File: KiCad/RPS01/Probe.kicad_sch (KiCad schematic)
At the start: 10 parts

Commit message: Finished Updating Footprints and Reorganized Reference Designators
Finished Updating Footprints and Reorganized Reference Designators

Starting to work on Final PCB, except for 19V Boost. Please check Schematic for errors
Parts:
- TP1: renamed from TP2; footprint (none) -> Mechatronics TestP:CONN1_RCU-0C_TEC
- TP10: value VSHUNT - -> VSHUNT-; footprint (none) -> Mechatronics TestP:CONN1_RCU-0C_TEC
- TP2: renamed from TP3; footprint (none) -> Mechatronics TestP:CONN1_RCU-0C_TEC
- TP3: renamed from TP4; footprint (none) -> Mechatronics TestP:CONN1_RCU-0C_TEC
- TP4: renamed from TP5; footprint (none) -> Mechatronics TestP:CONN1_RCU-0C_TEC
- TP5: renamed from TP6; footprint (none) -> Mechatronics TestP:CONN1_RCU-0C_TEC
- TP6: renamed from TP7; footprint (none) -> Mechatronics TestP:CONN1_RCU-0C_TEC
- TP7: renamed from TP1; footprint (none) -> Mechatronics TestP:CONN1_RCU-0C_TEC
- TP8: footprint (none) -> Mechatronics TestP:CONN1_RCU-0C_TEC
- TP9: value VSHUNT + -> VSHUNT+; footprint (none) -> Mechatronics TestP:CONN1_RCU-0C_TEC
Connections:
- net VSHUNT + renamed VSHUNT+
- net VSHUNT - renamed VSHUNT-
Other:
- moved on the sheet: TP10, TP9

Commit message: Hotfix
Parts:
- removed TP10: VSHUNT-, Mechatronics TestP:CONN1_RCU-0C_TEC, symbol Connector:TestPoint_Probe
- removed TP9: VSHUNT+, Mechatronics TestP:CONN1_RCU-0C_TEC, symbol Connector:TestPoint_Probe
- renumbered TP8 to TP10, TP1 to TP3, TP2 to TP4, TP3 to TP5, TP4 to TP6, TP5 to TP7, TP6 to TP8, TP7 to TP9

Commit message: Progress
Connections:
- net AREF: no longer TP9.1
- net CURRENT1: no longer TP5.1
- net CURRENT2: no longer TP6.1
- net LOGIC 5V: no longer TP10.1
- net SCL: no longer TP4.1
- net SDA: no longer TP3.1
- net VOLT1: no longer TP7.1
- net VOLT2: no longer TP8.1
- no-connect marks 0 -> 16
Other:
- moved on the sheet: TP10, TP3, TP4, TP5, TP6, TP7, TP8, TP9

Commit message: Error Checker Complete
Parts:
- added TP13: VOLT1, Mechatronics TestP:CONN1_RCU-0C_TEC, symbol Connector:TestPoint_Probe
- added TP14: VOLT2, Mechatronics TestP:CONN1_RCU-0C_TEC, symbol Connector:TestPoint_Probe
- added TP15: AREF, Mechatronics TestP:CONN1_RCU-0C_TEC, symbol Connector:TestPoint_Probe
- added TP16, TP17: LOGIC 5V, Mechatronics TestP:CONN1_RCU-0C_TEC, symbol Connector:TestPoint_Probe
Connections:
- net AREF: now also TP9.1
- net CURRENT1: now also TP5.1
- net CURRENT2: now also TP6.1
- net LOGIC 5V: now also TP10.1
- net SCL: now also TP4.1
- net SDA: now also TP3.1
- net VOLT1: now also TP7.1
- net VOLT2: now also TP8.1
- new net +12V: TP15.1
- new net +19V: TP16.1
- new net +3.3V: TP13.1
- new net +5V: TP14.1
- new net GND: TP17.1
- no-connect marks 16 -> 0

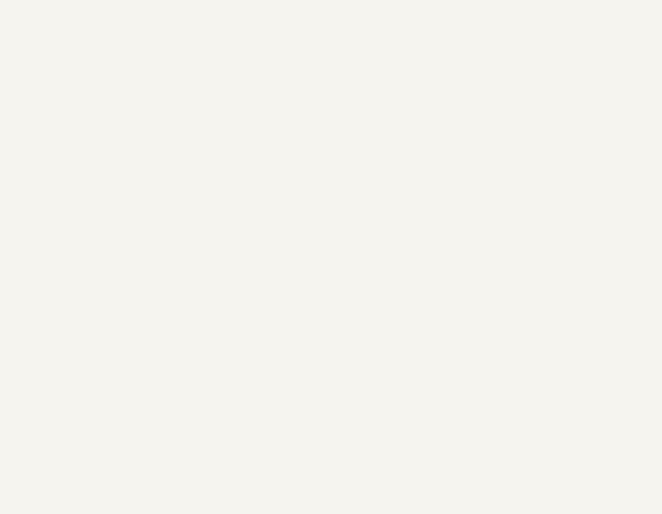
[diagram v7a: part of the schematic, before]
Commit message: Added Proper Mounting Holes and Updated PCB Dimensions
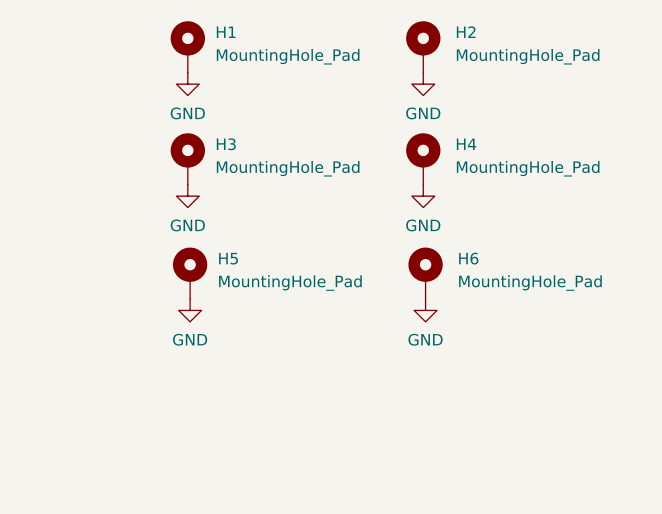
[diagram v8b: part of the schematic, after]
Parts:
- added H1, H2, H3, H4, H5, H6: MountingHole_Pad, MountingHole:MountingHole_3.2mm_M3_Pad_Via, symbol Mechanical:MountingHole_Pad
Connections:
- net GND: now also H1.1, H2.1, H3.1, H4.1, H5.1, H6.1
